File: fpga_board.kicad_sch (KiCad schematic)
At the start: 186 parts, among them Q1 2N7002PW, Q2 2N7002PW, Q3 2N7002PW, Q4 2N7002PW, Q5 2N7002PW, Q6 2N7002PW, SW1 1TS028A-1300-0600-CT, U1 LFE5U-45F-7BG256I, U10 TLV62569DRL, U2 CYUSB3014-BZXC, U3 TLV62569DRL, U5 K4B4G1646E-BCMA, U6 K4B4G1646E-BCMA, U7 TLV62569DRL, U8 TLV62569DRL, U9 TLV62569DRL, X1 XO32, Y1 Crystal_GND24

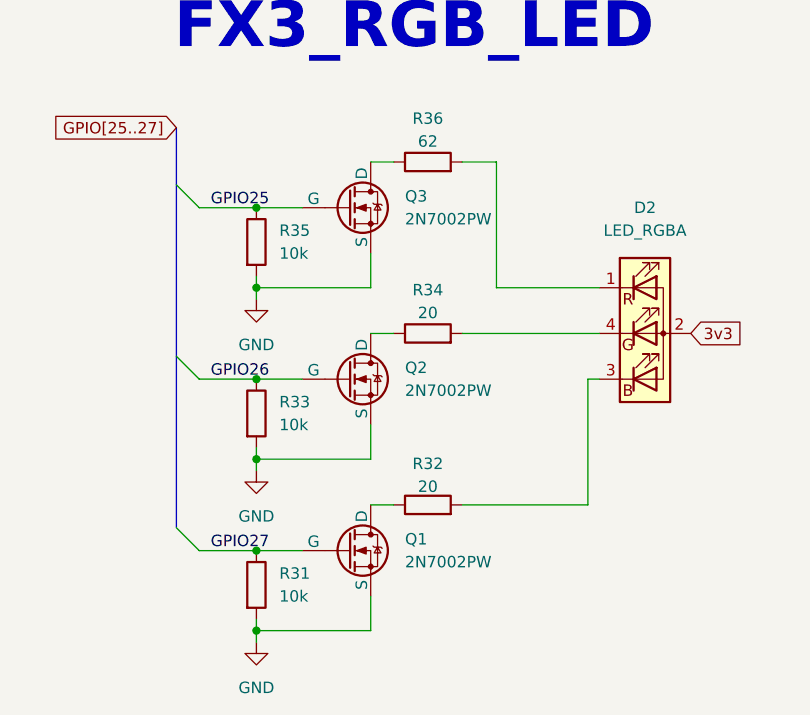
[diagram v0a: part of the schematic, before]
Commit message: FX decoupling and power finished
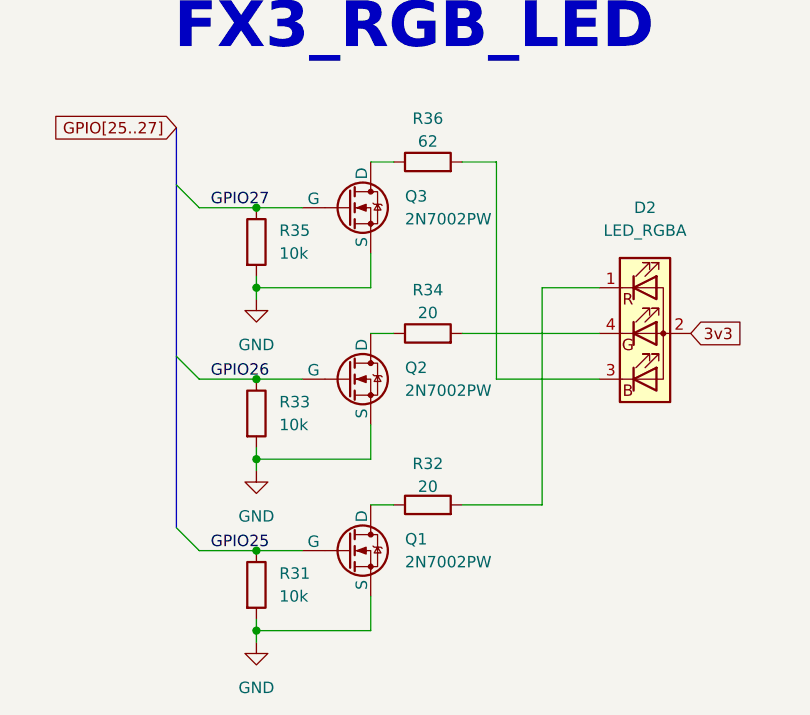
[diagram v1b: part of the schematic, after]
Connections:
- net GPIO25: now also Q1.2 (G), R31.1; no longer Q3.2 (G), R35.1
- net GPIO27: now also Q3.2 (G), R35.1; no longer Q1.2 (G), R31.1
- net at R36.2: now also D2.3 (BK); no longer D2.1 (RK)
- net at R32.2: now also D2.1 (RK); no longer D2.3 (BK)
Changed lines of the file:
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@@
 	(wire
 		(pts
+			(xy 697.23 367.03) (xy 708.66 367.03)
+		)
+		(stroke
+			(width 0)
+			(type default)
+		)
+	)
+	(wire
+		(pts
 			(xy 781.05 453.39) (xy 781.05 455.93)
 		)
@@
 	(wire
 		(pts
+			(xy 702.31 356.87) (xy 708.66 356.87)
+		)
+		(stroke
+			(width 0)
+			(type default)
+		)
+	)
+	(wire
+		(pts
 			(xy 335.28 256.54) (xy 358.14 256.54)
 		)
@@
 	(wire
 		(pts
+			(xy 702.31 356.87) (xy 702.31 381)
+		)
+		(stroke
+			(width 0)
+			(type default)
+		)
+	)
+	(wire
+		(pts
 			(xy 266.7 264.16) (xy 284.48 264.16)
 		)
@@
 	(wire
 		(pts
-			(xy 697.23 356.87) (xy 697.23 342.9)
+			(xy 697.23 342.9) (xy 697.23 367.03)
 		)
 		(stroke
@@
 	(wire
 		(pts
-			(xy 708.66 367.03) (xy 707.39 367.03)
-		)
-		(stroke
-			(width 0)
-			(type default)
-		)
-	)
-	(wire
-		(pts
 			(xy 138.43 435.61) (xy 140.97 435.61)
 		)
@@
 	(wire
 		(pts
-			(xy 707.39 367.03) (xy 707.39 381)
-		)
-		(stroke
-			(width 0)
-			(type default)
-		)
-	)
-	(wire
-		(pts
 			(xy 406.4 236.22) (xy 406.4 238.76)
 		)
@@
 	(wire
 		(pts
-			(xy 708.66 356.87) (xy 697.23 356.87)
-		)
-		(stroke
-			(width 0)
-			(type default)
-		)
-	)
-	(wire
-		(pts
 			(xy 170.18 384.81) (xy 175.26 384.81)
 		)
@@
 	(wire
 		(pts
-			(xy 707.39 381) (xy 693.42 381)
+			(xy 702.31 381) (xy 693.42 381)
 		)
 		(stroke
@@
 	)
 	(label "GPIO25"
-		(at 665.48 347.98 0)
+		(at 665.48 386.08 0)
 		(effects
 			(font
@@
 	)
 	(label "GPIO27"
-		(at 665.48 386.08 0)
+		(at 665.48 347.98 0)
 		(effects
 			(font

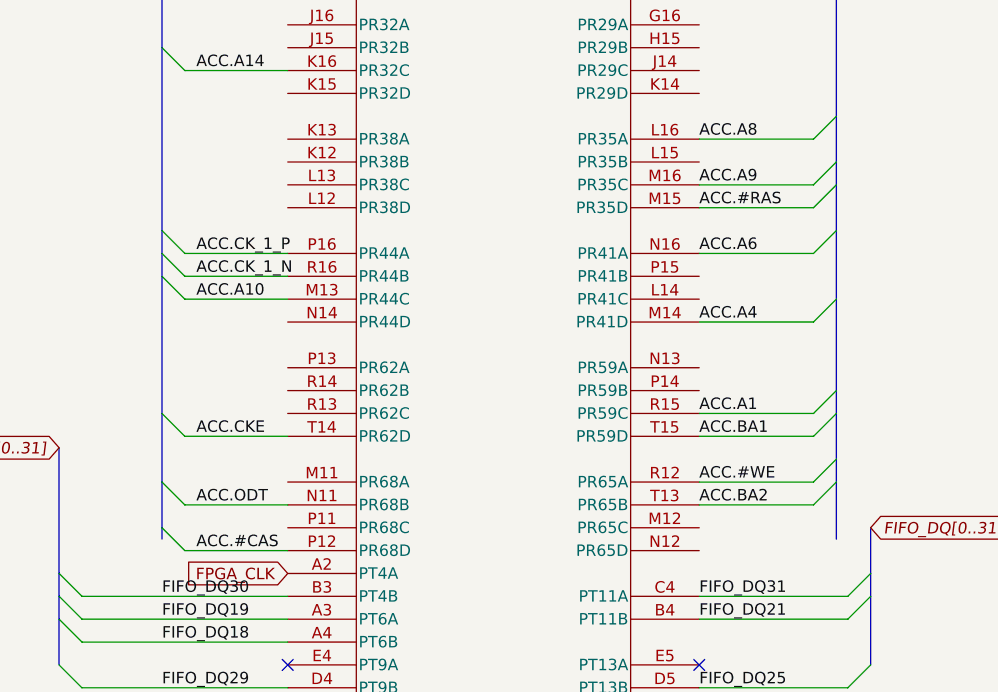
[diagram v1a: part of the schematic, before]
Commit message: fixed ACC length matching on B.Cu and F.Cu.
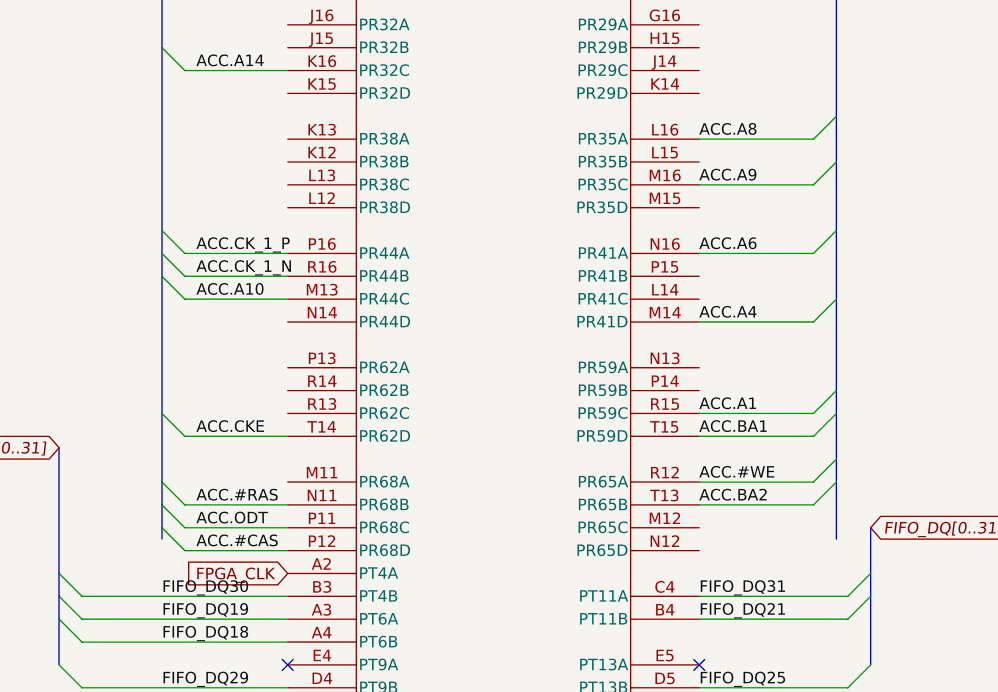
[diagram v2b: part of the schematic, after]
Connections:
- net ACC.#RAS: now also U1.N11 (PR68B); no longer U1.M15 (PR35D)
- net ACC.ODT: now also U1.P11 (PR68C); no longer U1.N11 (PR68B)
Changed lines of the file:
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@@
 	)
 	(bus_entry
-		(at 311.15 534.67)
+		(at 311.15 537.21)
 		(size 2.54 2.54)
 		(stroke
@@
 	)
 	(bus_entry
-		(at 386.08 501.65)
-		(size -2.54 2.54)
+		(at 311.15 534.67)
+		(size 2.54 2.54)
 		(stroke
 			(width 0)
@@
 	(bus
 		(pts
-			(xy 386.08 501.65) (xy 386.08 506.73)
-		)
-		(stroke
-			(width 0)
-			(type default)
-		)
-	)
-	(bus
-		(pts
 			(xy 661.67 160.02) (xy 661.67 162.56)
 		)
@@
 	(bus
 		(pts
-			(xy 386.08 499.11) (xy 386.08 501.65)
+			(xy 386.08 499.11) (xy 386.08 506.73)
 		)
 		(stroke
@@
 	(wire
 		(pts
-			(xy 370.84 504.19) (xy 383.54 504.19)
-		)
-		(stroke
-			(width 0)
-			(type default)
-		)
-	)
-	(wire
-		(pts
 			(xy 702.31 356.87) (xy 708.66 356.87)
 		)
@@
 		)
 	)
+	(bus
+		(pts
+			(xy 311.15 534.67) (xy 311.15 537.21)
+		)
+		(stroke
+			(width 0)
+			(type default)
+		)
+	)
 	(wire
 		(pts
@@
 		)
 	)
+	(bus
+		(pts
+			(xy 311.15 537.21) (xy 311.15 539.75)
+		)
+		(stroke
+			(width 0)
+			(type default)
+		)
+	)
 	(wire
 		(pts
@@
 		)
 	)
-	(bus
-		(pts
-			(xy 311.15 534.67) (xy 311.15 539.75)
-		)
-		(stroke
-			(width 0)
-			(type default)
-		)
-	)
 	(wire
 		(pts
@@
 	(wire
 		(pts
-			(xy 313.69 537.21) (xy 325.12 537.21)
+			(xy 313.69 539.75) (xy 325.12 539.75)
 		)
 		(stroke
@@
 	(wire
 		(pts
+			(xy 313.69 537.21) (xy 325.12 537.21)
+		)
+		(stroke
+			(width 0)
+			(type default)
+		)
+	)
+	(wire
+		(pts
 			(xy 683.26 394.97) (xy 683.26 391.16)
 		)
@@
 	)
 	(label "ACC.ODT"
-		(at 314.96 537.21 0)
+		(at 314.96 539.75 0)
 		(effects
 			(font
@@
 	)
 	(label "ACC.#RAS"
-		(at 370.84 504.19 0)
+		(at 314.96 537.21 0)
 		(effects
 			(font

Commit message: DDR3 decoupling finished.
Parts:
- added C100, C101, C102, C103, C104, C105, C106, C107, C108, C109, C110, C111, C112, C113, C96, C97, C98, C99: 0.1µF, Capacitor_SMD:C_0402_1005Metric, symbol Device:C
- C42, C43: value 4.7µF -> 0.1µF
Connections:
- net 1v35: now also C42.2, C43.2, C100.2, C101.2, C102.2, C103.2, C104.2, C105.2, C106.2, C107.2, C108.2, C109.2, C110.2, C111.2, C112.2, C113.2, C96.2, C97.2, C98.2, C99.2; no longer C42.1, C43.1
- net GND: now also C42.1, C43.1, C100.1, C101.1, C102.1, C103.1, C104.1, C105.1, C106.1, C107.1, C108.1, C109.1, C110.1, C111.1, C112.1, C113.1, C96.1, C97.1, C98.1, C99.1; no longer C42.2, C43.2
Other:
- note added: "DDR3 Decoupling"
- note removed: "Just add however much capacitors decoupling I can fit here"
- moved on the sheet: C38, C39, C40, C41, C56, R30, SW1

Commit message: cosmetic siklscreen changes and moved some footprints for better silkscreen availability. Added another 0 ohm resistor for PMODE (PMODE_2). Labeled configuration resistors.
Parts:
- added R5: 0, Resistor_SMD:R_0402_1005Metric, symbol Device:R
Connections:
- net at U2.L4 (GPIO[32]): now also R5.2
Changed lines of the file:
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@@
 	)
 	(no_connect
-		(at 678.18 139.7)
-	)
-	(no_connect
 		(at 527.05 104.14)
 	)
@@
 	)
 	(no_connect
+		(at 666.75 139.7)
+	)
+	(no_connect
 		(at 527.05 137.16)
 	)
@@
 		)
 	)
+	(wire
+		(pts
+			(xy 674.37 139.7) (xy 678.18 139.7)
+		)
+		(stroke
+			(width 0)
+			(type default)
+		)
+	)
 	(bus
 		(pts
@@
 		(dnp no)
 		(property "Reference" "R3"
-			(at 664.972 137.668 90)
+			(at 674.878 133.35 90)
 			(effects
 				(font
@@
 		)
 		(property "Value" "0"
-			(at 664.972 135.636 90)
+			(at 677.926 133.35 90)
 			(effects
 				(font
@@
 		(dnp no)
 		(property "Reference" "R4"
-			(at 669.29 139.446 90)
+			(at 674.878 135.89 90)
 			(effects
 				(font
@@
 		)
 		(property "Value" "0"
-			(at 672.338 139.446 90)
+			(at 677.926 135.89 90)
 			(effects
 				(font
@@
 					(unit 1)
 				)
+			)
+		)
+	)
+	(symbol
+		(lib_id "Device:R")
+		(at 670.56 139.7 90)
+		(unit 1)
+		(exclude_from_sim no)
+		(in_bom yes)
+		(on_board yes)
+		(dnp no)
+		(property "Reference" "R5"
+			(at 674.878 138.43 90)
+			(effects
+				(font
+					(size 1.27 1.27)
+				)
+			)
+		)
+		(property "Value" "0"
+			(at 677.926 138.43 90)
+			(effects
+				(font
+					(size 1.27 1.27)
+				)
+			)
+		)
+		(property "Footprint" "Resistor_SMD:R_0402_1005Metric"
+			(at 670.56 141.478 90)
+			(effects
+				(font
+					(size 1.27 1.27)
+				)
+				(hide yes)
+			)
+		)
+		(property "Datasheet" "https://www.lcsc.com/datasheet/C106231.pdf"
+			(at 670.56 139.7 0)
+			(effects
+				(font
+					(size 1.27 1.27)
+				)
+				(hide yes)
+			)
+		)
+		(property "Description" "Resistor"
+			(at 670.56 139.7 0)
+			(effects
+				(font
+					(size 1.27 1.27)
+				)
+				(hide yes)
+			)
+		)
+		(pin "2"
+		)
+		(pin "1"
+		)
+		(instances
+			(project "fpga_board"
+				(path "/5c9167d7-9fb7-40fb-893a-3a7eaf125f07"
+					(reference "R5")
+					(unit 1)
+				)

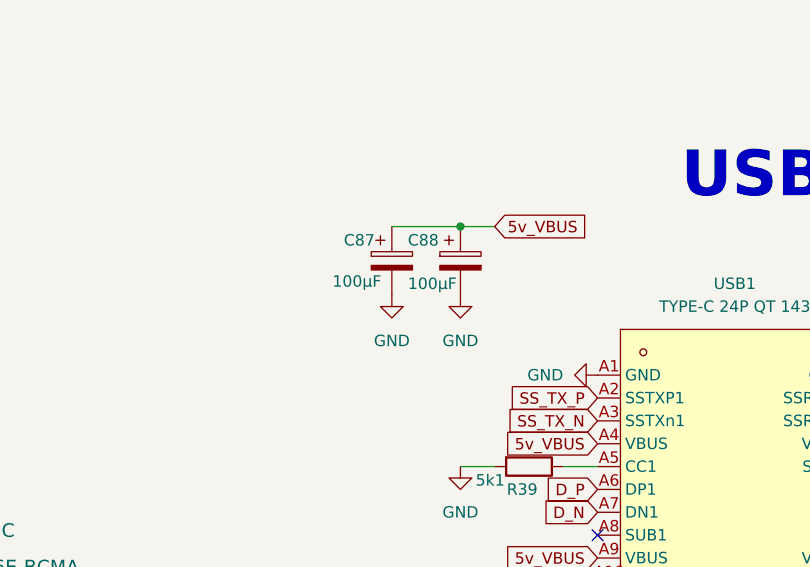
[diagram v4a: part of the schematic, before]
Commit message: Added Another 100μF capacitor because I have empty space why not plus it looks cooler
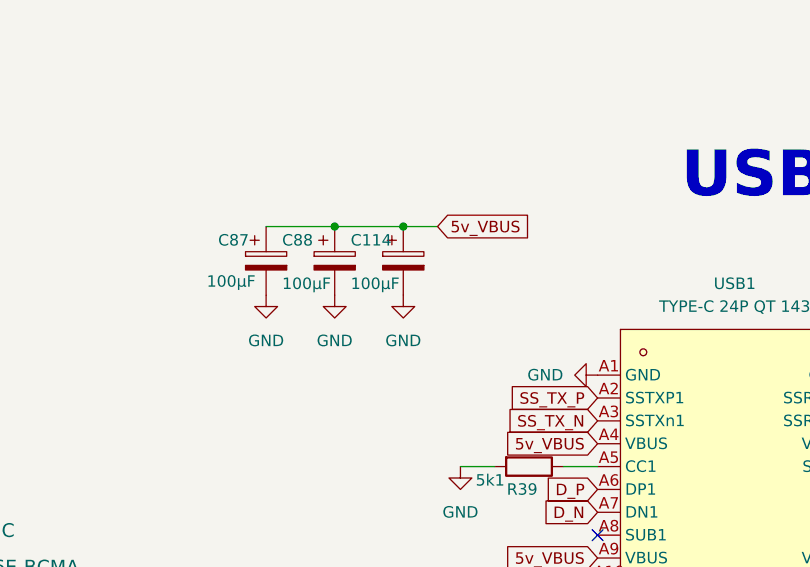
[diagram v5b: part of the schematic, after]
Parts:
- added C114: 100μF, Capacitor_SMD:CP_Elec_6.3x5.4, symbol Device:C_Polarized
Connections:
- net 5v_VBUS: now also C114.1
- net GND: now also C114.2
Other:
- moved on the sheet: C87, C88
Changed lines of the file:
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@@
 	)
 	(junction
-		(at 521.97 185.42)
+		(at 508 185.42)
 		(diameter 0)
 		(color 0 0 0 0)
@@
 	)
 	(junction
+		(at 515.62 185.42)
+		(diameter 0)
+		(color 0 0 0 0)
+	)
+	(junction
 		(at 99.06 113.03)
 		(diameter 0)
@@
 	(wire
 		(pts
-			(xy 521.97 185.42) (xy 525.78 185.42)
+			(xy 508 185.42) (xy 515.62 185.42)
 		)
 		(stroke
@@
 	(wire
 		(pts
-			(xy 514.35 185.42) (xy 521.97 185.42)
+			(xy 500.38 185.42) (xy 508 185.42)
 		)
 		(stroke
@@
 	(wire
 		(pts
+			(xy 515.62 185.42) (xy 519.43 185.42)
+		)
+		(stroke
+			(width 0)
+			(type default)
+		)
+	)
+	(wire
+		(pts
 			(xy 287.02 406.4) (xy 287.02 405.13)
 		)
@@
 	(global_label "5v_VBUS"
 		(shape input)
-		(at 525.78 185.42 0)
+		(at 519.43 185.42 0)
 		(fields_autoplaced yes)
 		(effects
@@
 		)
 		(property "Intersheetrefs" "${INTERSHEET_REFS}"
-			(at 536.8085 185.42 0)
+			(at 530.4585 185.42 0)
 			(effects
 				(font
@@
 	)
 	(symbol
+		(lib_id "Device:C_Polarized")
+		(at 515.62 189.23 0)
+		(unit 1)
+		(exclude_from_sim no)
+		(in_bom yes)
+		(on_board yes)
+		(dnp no)
+		(property "Reference" "C114"
+			(at 509.778 186.944 0)
+			(effects
+				(font
+					(size 1.27 1.27)
+				)
+				(justify left)
+			)
+		)
+		(property "Value" "100μF"
+			(at 509.778 191.77 0)
+			(effects
+				(font
+					(size 1.27 1.27)
+				)
+				(justify left)
+			)
+		)
+		(property "Footprint" "Capacitor_SMD:CP_Elec_6.3x5.4"
+			(at 516.5852 193.04 0)
+			(effects
+				(font
+					(size 1.27 1.27)
+				)
+				(hide yes)
+			)
+		)
+		(property "Datasheet" "https://www.lcsc.com/datasheet/C2887276.pdf"
+			(at 515.62 189.23 0)
+			(effects
+				(font
+					(size 1.27 1.27)
+				)
+				(hide yes)
+			)
+		)
+		(property "Description" "Polarized capacitor"
+			(at 515.62 189.23 0)
+			(effects
+				(font
+					(size 1.27 1.27)
+				)
+				(hide yes)
+			)
+		)
+		(pin "1"
+		)
+		(pin "2"
+		)
+		(instances
+			(project "fpga_board"
+				(path "/5c9167d7-9fb7-40fb-893a-3a7eaf125f07"
+					(reference "C114")
+					(unit 1)
+				)
+			)
+		)
+	)
+	(symbol
 		(lib_id "Device:C")
 		(at 732.79 453.39 0)
@@
 	(symbol
 		(lib_id "Device:C_Polarized")
-		(at 521.97 189.23 0)
+		(at 508 189.23 0)
 		(unit 1)
 		(exclude_from_sim no)
@@
 		(dnp no)
 		(property "Reference" "C88"
-			(at 516.128 186.944 0)
+			(at 502.158 186.944 0)
 			(effects
 				(font
@@
 		)
 		(property "Value" "100μF"
-			(at 516.128 191.77 0)
+			(at 502.158 191.77 0)
 			(effects
 				(font
@@
 		)
 		(property "Footprint" "Capacitor_SMD:CP_Elec_6.3x5.4"
-			(at 522.9352 193.04 0)
+			(at 508.9652 193.04 0)
 			(effects
 				(font
@@
 		)
 		(property "Datasheet" "https://www.lcsc.com/datasheet/C2887276.pdf"
-			(at 521.97 189.23 0)
+			(at 508 189.23 0)
 			(effects
 				(font
@@
 		)
 		(property "Description" "Polarized capacitor"
-			(at 521.97 189.23 0)
+			(at 508 189.23 0)
 			(effects
 				(font
@@
 	(symbol
 		(lib_id "power:GND")
-		(at 521.97 193.04 0)
+		(at 508 193.04 0)
 		(unit 1)
 		(exclude_from_sim no)
@@
 		(fields_autoplaced yes)
 		(property "Reference" "#PWR0112"
-			(at 521.97 199.39 0)
+			(at 508 199.39 0)
 			(effects
 				(font
@@
 		)
 		(property "Value" "GND"
-			(at 521.97 198.12 0)
+			(at 508 198.12 0)
 			(effects
 				(font
@@
 		)
 		(property "Footprint" ""
-			(at 521.97 193.04 0)
+			(at 508 193.04 0)
 			(effects
 				(font
@@
 		)
 		(property "Datasheet" ""
-			(at 521.97 193.04 0)
+			(at 508 193.04 0)
 			(effects
 				(font
@@
 		)
 		(property "Description" "Power symbol creates a global label with name \"GND\" , ground"
-			(at 521.97 193.04 0)
+			(at 508 193.04 0)
 			(effects
 				(font
@@
 	(symbol
 		(lib_id "Device:C_Polarized")
-		(at 514.35 189.23 0)
+		(at 500.38 189.23 0)
 		(unit 1)
 		(exclude_from_sim no)
@@
 		(dnp no)
 		(property "Reference" "C87"
-			(at 509.016 186.944 0)
+			(at 495.046 186.944 0)
 			(effects
 				(font
@@
 		)
 		(property "Value" "100μF"
-			(at 507.746 191.516 0)
+			(at 493.776 191.516 0)
 			(effects
 				(font
@@
 		)
 		(property "Footprint" "Capacitor_SMD:CP_Elec_6.3x5.4"
-			(at 515.3152 193.04 0)
+			(at 501.3452 193.04 0)
 			(effects
 				(font
@@
 		)
 		(property "Datasheet" "https://www.lcsc.com/datasheet/C2887276.pdf"
-			(at 514.35 189.23 0)
+			(at 500.38 189.23 0)
 			(effects
 				(font
@@
 		)
 		(property "Description" "Polarized capacitor"
-			(at 514.35 189.23 0)
+			(at 500.38 189.23 0)
 			(effects
 				(font
@@
 	)
 	(symbol
+		(lib_id "power:GND")
+		(at 515.62 193.04 0)
+		(unit 1)
+		(exclude_from_sim no)
+		(in_bom yes)
+		(on_board yes)
+		(dnp no)
+		(fields_autoplaced yes)
+		(property "Reference" "#PWR044"
+			(at 515.62 199.39 0)
+			(effects
+				(font
+					(size 1.27 1.27)
+				)
+				(hide yes)
+			)
+		)
+		(property "Value" "GND"
+			(at 515.62 198.12 0)
+			(effects
+				(font
+					(size 1.27 1.27)
+				)
+			)
+		)
+		(property "Footprint" ""
+			(at 515.62 193.04 0)
+			(effects
+				(font
+					(size 1.27 1.27)
+				)
+				(hide yes)
+			)
+		)
+		(property "Datasheet" ""
+			(at 515.62 193.04 0)
+			(effects
+				(font
+					(size 1.27 1.27)
+				)
+				(hide yes)
+			)
+		)
+		(property "Description" "Power symbol creates a global label with name \"GND\" , ground"
+			(at 515.62 193.04 0)
+			(effects
+				(font
+					(size 1.27 1.27)
+				)
+				(hide yes)
+			)
+		)
+		(pin "1"
+		)
+		(instances
+			(project "fpga_board"
+				(path "/5c9167d7-9fb7-40fb-893a-3a7eaf125f07"
+					(reference "#PWR044")
+					(unit 1)
+				)
+			)
+		)
+	)
+	(symbol
 		(lib_id "Device:R")
 		(at 144.78 440.69 90)
@@
 	(symbol
 		(lib_id "power:GND")
-		(at 514.35 193.04 0)
+		(at 500.38 193.04 0)
 		(unit 1)
 		(exclude_from_sim no)
@@
 		(fields_autoplaced yes)
 		(property "Reference" "#PWR091"
-			(at 514.35 199.39 0)
+			(at 500.38 199.39 0)
 			(effects
 				(font
@@
 		)
 		(property "Value" "GND"
-			(at 514.35 198.12 0)
+			(at 500.38 198.12 0)
 			(effects
 				(font
@@
 		)
 		(property "Footprint" ""
-			(at 514.35 193.04 0)
+			(at 500.38 193.04 0)
 			(effects
 				(font
@@
 		)
 		(property "Datasheet" ""
-			(at 514.35 193.04 0)
+			(at 500.38 193.04 0)
 			(effects
 				(font
@@
 		)
 		(property "Description" "Power symbol creates a global label with name \"GND\" , ground"
-			(at 514.35 193.04 0)
+			(at 500.38 193.04 0)
 			(effects
 				(font

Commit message: changed some component values to reduce BOM cost, updated sheets for out of stock components.
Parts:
- C1, C10, C100, C101, C102, C103, C104, C105, C106, C107, C108, C109, C110, C111, C112, C113, C12, C13, C14, C16, C17, C2, C20, C21, C24, C25, C3, C38, C39, C40, C41, C42, C43, C44, C45, C46, C47, C48, C49, C50, C51, C52, C56, C57, C58, C59, C6, C60, C62, C65, C67, C68, C69, C70, C71, C72, C77, C78, C79, C81, C83, C84, C85, C91, C92, C93, C94, C95, C96, C97, C98, C99: LCSC Part (none) -> C60474
- C11, C18, C19, C22, C23, C26, C8, C89, C9, C90: LCSC Part (none) -> C22435944
- C114, C87, C88: LCSC Part (none) -> C2887276
- C15: value 2.2µF -> 4.7µF; Internal.R (none) -> 8m2Ω; LCSC Part (none) -> C6119786
- C27, C28: LCSC Part (none) -> C5448865
- C29, C31, C33, C35, C37, C63: LCSC Part (none) -> C6119786
- C30, C32, C34, C36, C64: LCSC Part (none) -> C6119814
- C4, C5, C53, C54, C55, C66, C7, C80, C82: LCSC Part (none) -> C6119868
- C61: value 2.2nF -> 0.01µF; LCSC Part (none) -> C22435944
- C73, C74, C75, C76, C86: LCSC Part (none) -> C315248
- D1, D2: LCSC Part (none) -> C22461780
- FB1: LCSC Part (none) -> C307770
- L1, L2, L3, L4: LCSC Part (none) -> C85833
- L5, L6, L7, L8, L9: LCSC Part (none) -> C42924311
- Q1, Q2, Q3, Q4, Q5, Q6: LCSC Part (none) -> C7379955
- R1: LCSC Part (none) -> C168240
- R10, R12, R14, R16, R38, R53, R9: LCSC Part (none) -> C14675
- R11: LCSC Part (none) -> C3013201
- R13: LCSC Part (none) -> C3016392
- R15: LCSC Part (none) -> C2999460
- R17, R23, R25, R28, R29: LCSC Part (none) -> C3017492
- R18, R19, R26, R27, R3, R4, R5, R6, R7, R8: LCSC Part (none) -> C106231
- R2: LCSC Part (none) -> C25087
- R20, R21, R24: LCSC Part (none) -> C22548
- R22, R37: LCSC Part (none) -> C49653074
- R30, R31, R33, R35, R41, R42, R43: LCSC Part (none) -> C51035904
- R32, R34, R45, R46, R47: LCSC Part (none) -> C3017453
- R36, R44: LCSC Part (none) -> C49653021
- R39: LCSC Part (none) -> C49652827
- R40: LCSC Part (none) -> C2906929
- R48, R49, R50, R51: LCSC Part (none) -> C853312; Tol (none) -> 1%
- R52: LCSC Part (none) -> C20165692
- U1: value LFE5U-45F-7BG256I -> LFE5U-45F-6BG256C; LCSC Part (none) -> C1550834
- U10, U3, U7, U8, U9: LCSC Part (none) -> C163217
- U2: LCSC Part (none) -> C462526
- U5, U6: value K4B4G1646E-BCMA -> MT41K256M16TW-093:P; LCSC Part (none) -> C2064402
- X1: LCSC Part (none) -> C50345411
- Y1: LCSC Part (none) -> C7206296
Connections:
- net GND: now also C15.2, C61.1; no longer C15.1, C61.2
- net at C16.2, L1.2, U2.A7 (AVDD): now also C15.1; no longer C15.2
- net at R38.1, USB1.15 (EP), USB1.16 (EP)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: now also C61.2; no longer C61.1
